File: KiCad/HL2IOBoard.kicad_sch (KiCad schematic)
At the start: 117 parts, among them J1 Conn_02x25_Odd_Even, J10 142-0701-851, J12 Conn_02x01, J2 Conn_01x05, J3 FAN, J4 Conn_02x04_Odd_Even, J5 LD09P13A4GX00LF, J6 Conn_02x04_Odd_Even, J7 Conn_01x09, J8 Conn_01x05, J9 142-0701-851, P1 TestPoint, P2 TestPoint, P3 TestPoint, P4 TestPoint, Q1 NUD3160LT1G, Q2 SSM3J374R,LF, Q3 SSM3J374R,LF, Q4 BC847C-13-F, Q5 BC847C-13-F, Q6 FCX491ATA, Sw12 TestPoint, Sw5 TestPoint, T1 TestPoint, T2 TestPoint, T4 TestPoint, T5 TestPoint, T6 TestPoint, U1 Pico, U11 PCA9536D, U13 TLV9351IDCKR, U2 MASWSS0179TR-3000, U3 MASWSS0179TR-3000, U4 MASWSS0179TR-3000, U5 AS78L05RTR-E1, U6 MC74HCT04ADR2G, U7 74HCT541PW,118, U8 TBD62381AFWG,EL, U9 LM4040DIM3X-3.0/NOPB

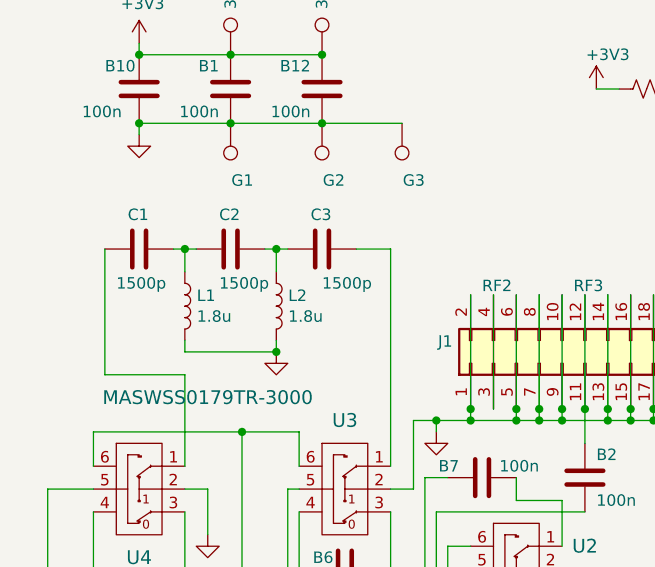
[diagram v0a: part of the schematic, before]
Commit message: Add the IO board control program.
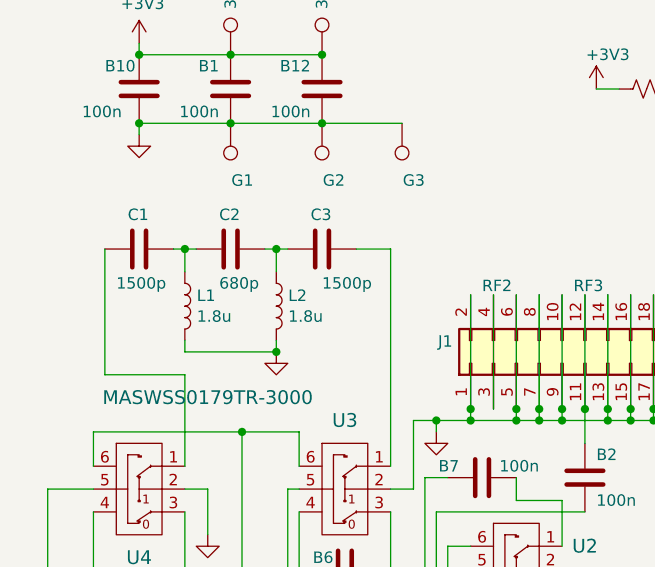
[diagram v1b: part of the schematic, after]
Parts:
- C2: value 1500p -> 680p
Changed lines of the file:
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@@
   (title_block
     (title "Hermes Lite2 IO Connector")
-    (date "2023-03-26")
-    (rev "E")
+    (date "2023-09-12")
+    (rev "F")
     (company "N2ADR")
   )
@@
       (effects (font (size 1.27 1.27)) (justify left))
     )
-    (property "Value" "1500p" (id 1) (at 33.02 49.53 90)
+    (property "Value" "680p" (id 1) (at 33.02 49.53 90)
       (effects (font (size 1.27 1.27)) (justify left))
     )
@@
     )
     (path "/00000000-0000-0000-0000-0000620251cd"
-      (reference "C2") (unit 1) (value "1500p") (footprint "Capacitor_SMD:C_0805_2012Metric_Pad1.18x1.45mm_HandSolder")
+      (reference "C2") (unit 1) (value "680p") (footprint "Capacitor_SMD:C_0805_2012Metric_Pad1.18x1.45mm_HandSolder")
     )
     (path "/00000000-0000-0000-0000-000062025c4b"

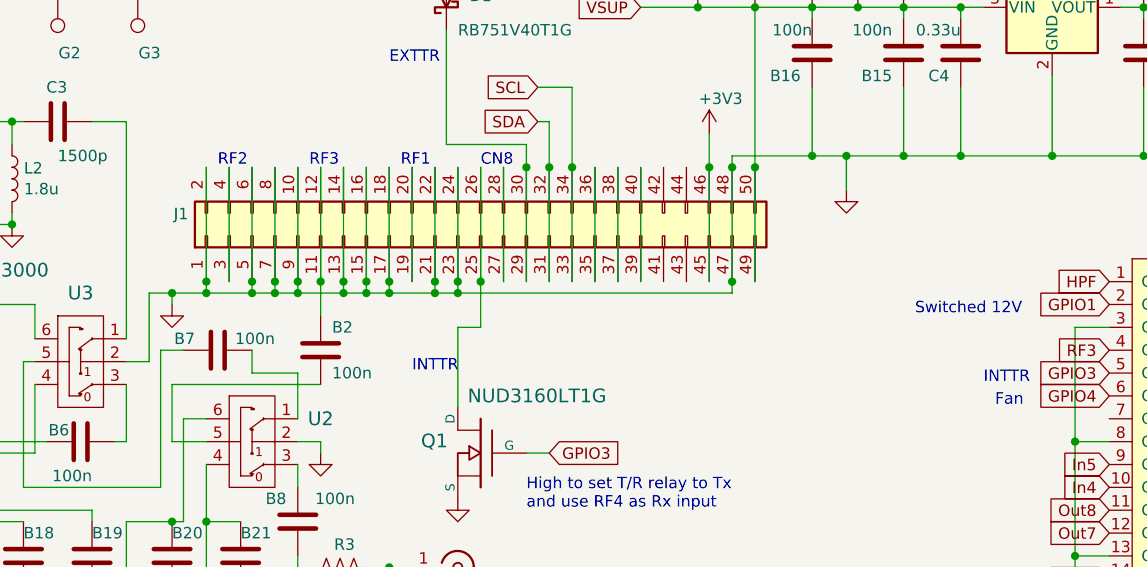
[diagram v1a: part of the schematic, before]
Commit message: Change 2x25 connector J1 from 13.59 to 11.05 mm insulation height.
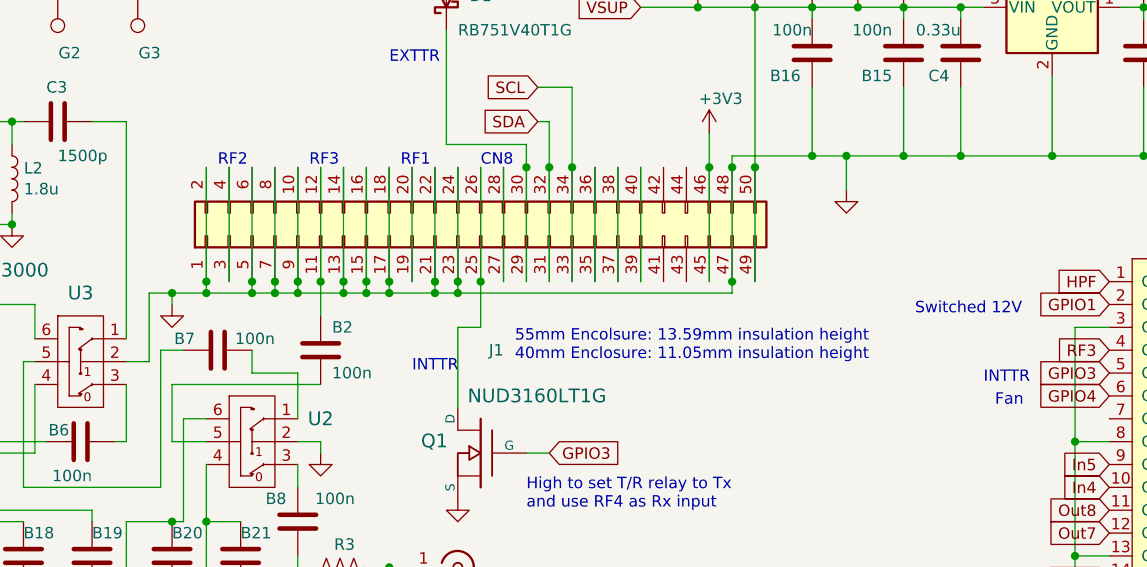
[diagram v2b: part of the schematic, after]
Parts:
- J1: P/N 2047-2X25G00S3U -> 2047-2X25G00S1U
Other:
- note added: "55mm Encolsure: 13.59mm insulation height 40mm Enclosure: 11.05mm insulation height"
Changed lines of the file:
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@@
+    (effects (font (size 1.27 1.27)) (justify left bottom))
+  )
+  (text "55mm Encolsure: 13.59mm insulation height\n40mm Enclosure: 11.05mm insulation height"
+    (at 95.25 72.39 0)
     (effects (font (size 1.27 1.27)) (justify left bottom))
   )
@@
   (symbol (lib_id "Connector_Generic:Conn_02x25_Odd_Even") (at 91.44 58.42 90) (unit 1)
     (in_bom yes) (on_board yes)
-    (property "Reference" "J1" (id 0) (at 58.9534 55.9816 90)
+    (property "Reference" "J1" (id 0) (at 93.98 71.12 90)
       (effects (font (size 1.27 1.27)) (justify left))
     )
@@
       (effects (font (size 1.27 1.27)) hide)
     )
-    (property "P/N" "2047-2X25G00S3U" (id 4) (at 91.44 58.42 90)
-      (effects (font (size 1.27 1.27)) hide)
-    )
+    (property "P/N" "2047-2X25G00S1U" (id 4) (at 91.44 58.42 90)
+      (effects (font (size 1.27 1.27)) hide)
+    )
